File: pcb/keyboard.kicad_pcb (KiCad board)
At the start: 4 copper layers, 304.8 x 119.1 mm, 197 parts, among them J1 Conn_ARM_JTAG_SWD_10, J2 USB_C_Receptacle_USB2.0_16P, J3 Conn_Coaxial, K1 KEYSW, K10 KEYSW, K11 KEYSW, K12 KEYSW, K13 KEYSW, K14 KEYSW, K15 KEYSW, K16 KEYSW, K17 KEYSW, K18 KEYSW, K19 KEYSW, K2 KEYSW, K20 KEYSW, K21 KEYSW, K22 KEYSW, K23 KEYSW, K24 KEYSW, K25 KEYSW, K26 KEYSW, K27 KEYSW, K28 KEYSW, K29 KEYSW, K3 KEYSW, K30 KEYSW, K31 KEYSW, K32 KEYSW, K33 KEYSW, K34 KEYSW, K35 KEYSW, K36 KEYSW, K37 KEYSW, K38 KEYSW, K39 KEYSW, K4 KEYSW, K40 KEYSW, K41 KEYSW, K42 KEYSW, K43 KEYSW, K45 KEYSW, K46 KEYSW, K47 KEYSW, K48 KEYSW, K49 KEYSW, K5 KEYSW, K50 KEYSW, K51 KEYSW, K52 KEYSW, K53 KEYSW, K54 KEYSW, K55 KEYSW, K56 KEYSW, K57 KEYSW, K58 KEYSW, K59 KEYSW, K6 KEYSW, K60 KEYSW, K61 KEYSW, K62 KEYSW, K63 KEYSW, K67 KEYSW, K7 KEYSW, K70 KEYSW, K71 KEYSW, K72 KEYSW, K73 KEYSW, K74 KEYSW, K75 KEYSW, K8 KEYSW, K9 KEYSW, Q1 FDN340P, Q2 FS8025A, Q3 FDN340P, SW1 SW_SPST, SW2 SW_SPST, U1 nRF52840, U2 TP4056-42-ESOP8, U3 DW01A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

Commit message: Did some stuff
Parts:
- R10, R4, R5: footprint Resistor_SMD:R_0805_2012Metric_Pad1.20x1.40mm_HandSolder -> Resistor_SMD:R_0603_1608Metric_Pad0.98x0.95mm_HandSolder
- moved D65 250.8 mm to (81.0, 61.3)
- moved D66 250.8 mm to (81.0, 64.3)
- moved R5 222.4 mm to (74.5, 60.6)
- moved R4 217.5 mm to (74.4, 65.4)
- moved Q1 199.3 mm to (111.5, 63.7)
- moved Q3 199.3 mm to (111.5, 68.5)
- moved U2 199.3 mm to (119.0, 64.5)
- moved R10 180.9 mm to (233.4, 96.8), turned to 90 degrees
- moved R3 168.8 mm to (123.9, 54.5)
- moved F1 105.6 mm to (205.4, 56.4)
- moved C6 97.4 mm to (298.1, 84.5)
- moved C7 97.4 mm to (298.1, 87.5)
- moved C12 97.4 mm to (302.9, 78.5)
- moved C14 97.4 mm to (302.9, 84.5)
- moved C19 97.4 mm to (307.8, 72.5)
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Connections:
- D64 pad 1: Net-(D64-K) -> /power/BAT_POS
- F1 pad 1: Net-(Q1-D) -> Net-(SW2-B)
- F1 pad 2: Net-(BT1-+) -> Net-(Q1-D)
- Q1 pad 2: Net-(D64-K) -> /power/BAT_POS
- SW2 pad 1: Net-(D64-K) -> Net-(BT1-+)
- SW2 pad 2: /power/BAT_POS -> Net-(SW2-B)

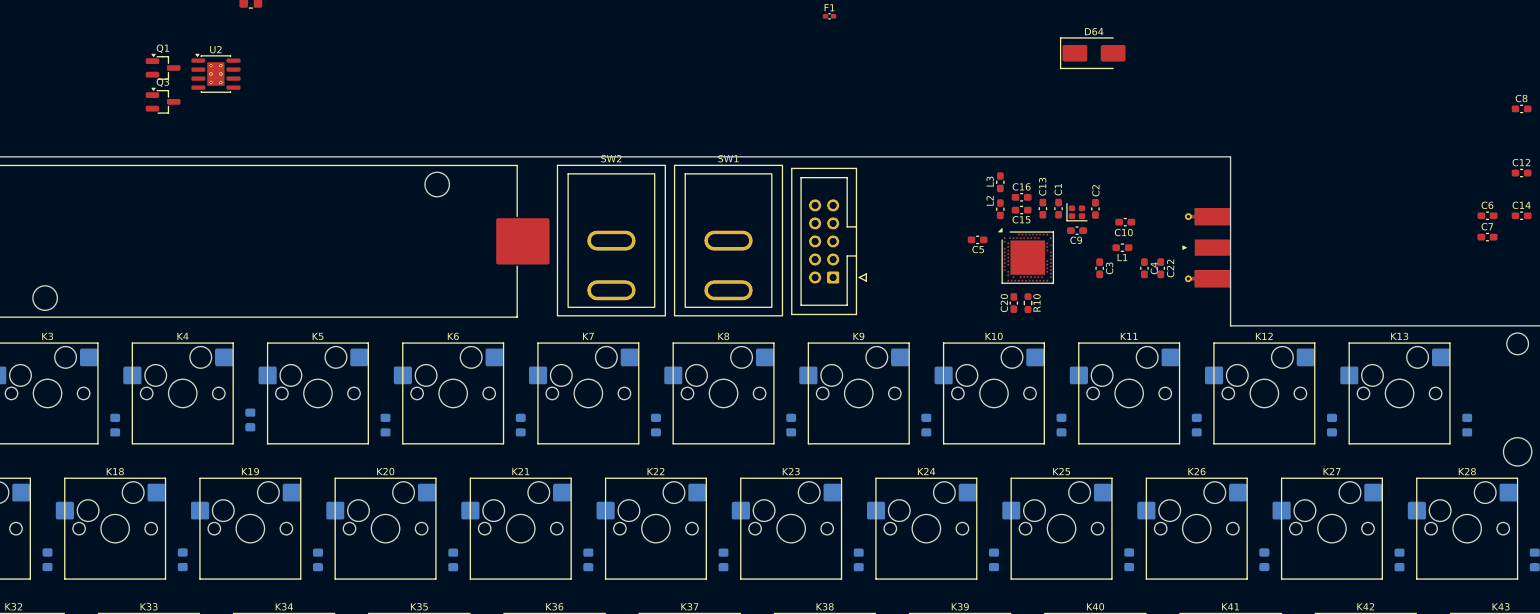
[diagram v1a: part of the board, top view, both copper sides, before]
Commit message: Fix diode placement
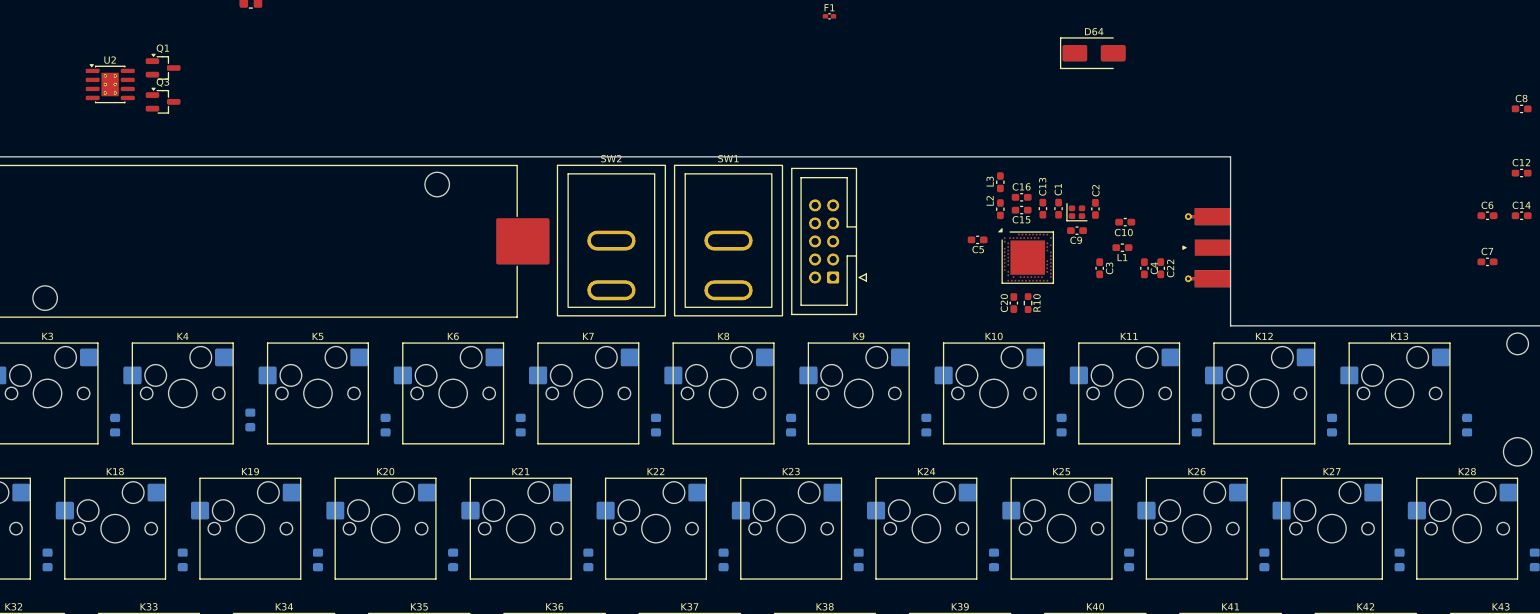
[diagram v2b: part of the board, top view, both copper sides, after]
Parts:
- moved D16 171.5 mm to (76.2, 133.0)
- moved D17 133.4 mm to (95.2, 133.0)
- moved D23 114.3 mm to (209.6, 133.0)
- moved D25 114.3 mm to (247.7, 133.0)
- moved D18 95.3 mm to (114.3, 133.0)
- moved D21 95.2 mm to (171.4, 133.0)
- moved D22 76.2 mm to (190.5, 133.0)
- moved D24 76.2 mm to (228.6, 133.0)
- moved D19 57.2 mm to (133.3, 133.0)
- moved D27 19.1 mm to (285.8, 133.0)
- moved D26 19.1 mm to (266.7, 133.0)
- moved D20 19.0 mm to (152.4, 133.0)
- moved U2 15.0 mm to (104.1, 66.0)
- moved C7 3.49 mm to (298.1, 91.0)

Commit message: Did a bunch of things!
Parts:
- C11, C17, C18, C23, D64, D68, F1, Q1, Q2, Q3, R11, R12, R13, R3, R6, R7, R8, R9, U3: moved to B.Cu
- D65, D66: footprint LED_SMD:LED_0805_2012Metric_Pad1.15x1.40mm_HandSolder -> LED_SMD:LED_0603_1608Metric_Pad1.05x0.95mm_HandSolder
- U2: footprint Package_SO:SOIC-8-1EP_3.9x4.9mm_P1.27mm_EP2.41x3.3mm_ThermalVias -> Package_SO:SOIC-8-1EP_3.9x4.9mm_P1.27mm_EP2.29x3mm; moved to B.Cu
- moved R13 191.6 mm to (99.6, 80.5)
- moved R12 178.5 mm to (107.1, 81.6)
- moved C17 173.4 mm to (129.2, 57.8), turned to 180 degrees
- moved C18 173.4 mm to (129.2, 60.8), turned to 180 degrees
- moved C23 171.9 mm to (92.7, 87.6), turned to 180 degrees
- moved D68 171.2 mm to (128.7, 39.9), turned to 180 degrees
- moved U3 171.0 mm to (128.8, 36.3), turned to 180 degrees
- moved R7 163.6 mm to (107.0, 85.4)
- moved Q2 160.0 mm to (134.3, 36.3), turned to 180 degrees
- moved C11 159.0 mm to (134.8, 40.0), turned to 180 degrees
- moved R11 137.1 mm to (145.8, 55.0), turned to 180 degrees
- moved R9 130.5 mm to (149.1, 48.9), turned to 180 degrees
- moved R8 109.6 mm to (159.6, 54.9), turned to 180 degrees
- moved R6 84.1 mm to (172.4, 52.4), turned to 180 degrees
- moved C19 84.1 mm to (225.9, 91.6), turned to 180 degrees
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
